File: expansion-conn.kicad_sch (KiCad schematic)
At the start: 6 parts, among them J1 J_ERM8-040-XX.X-X-DV-XX_SAMTEC

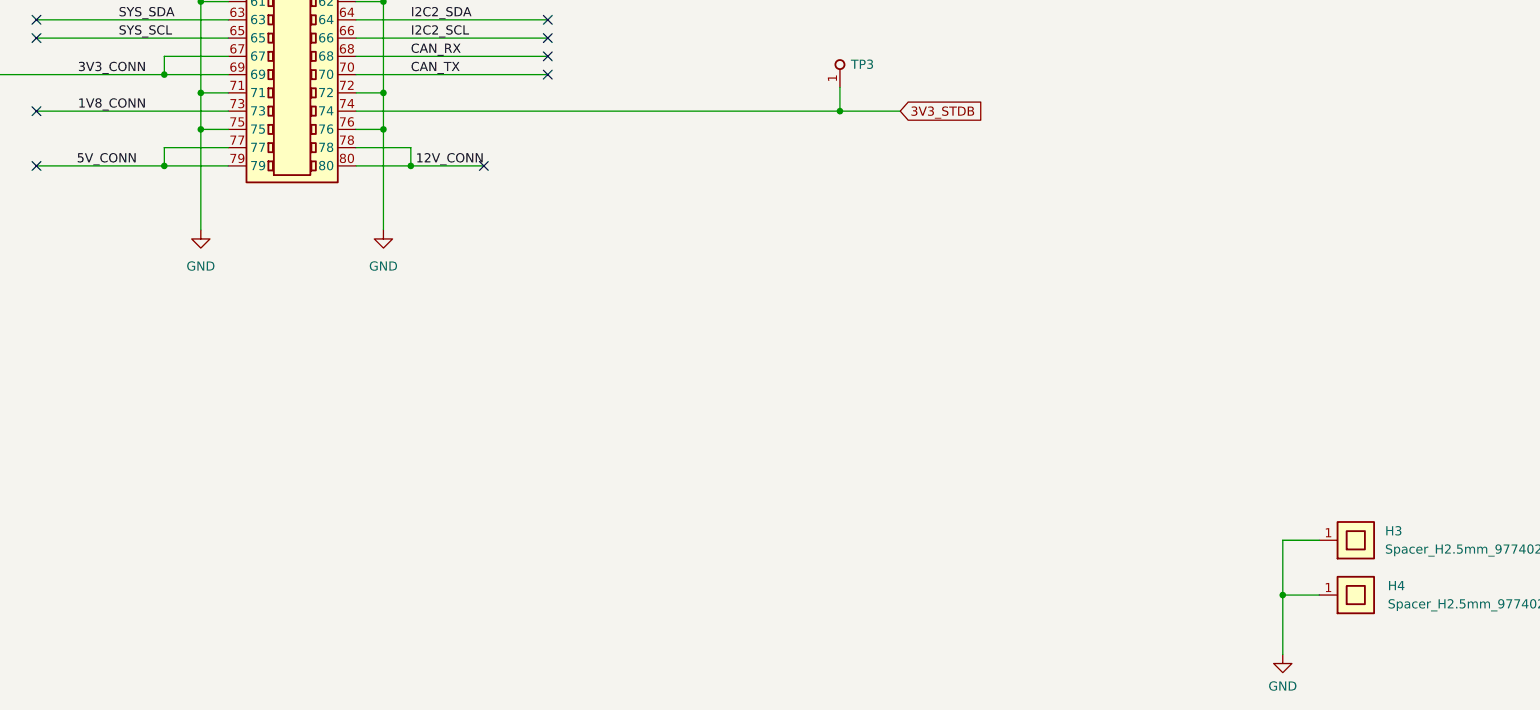
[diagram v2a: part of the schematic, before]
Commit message: [#45990] Fix silk screen drcs
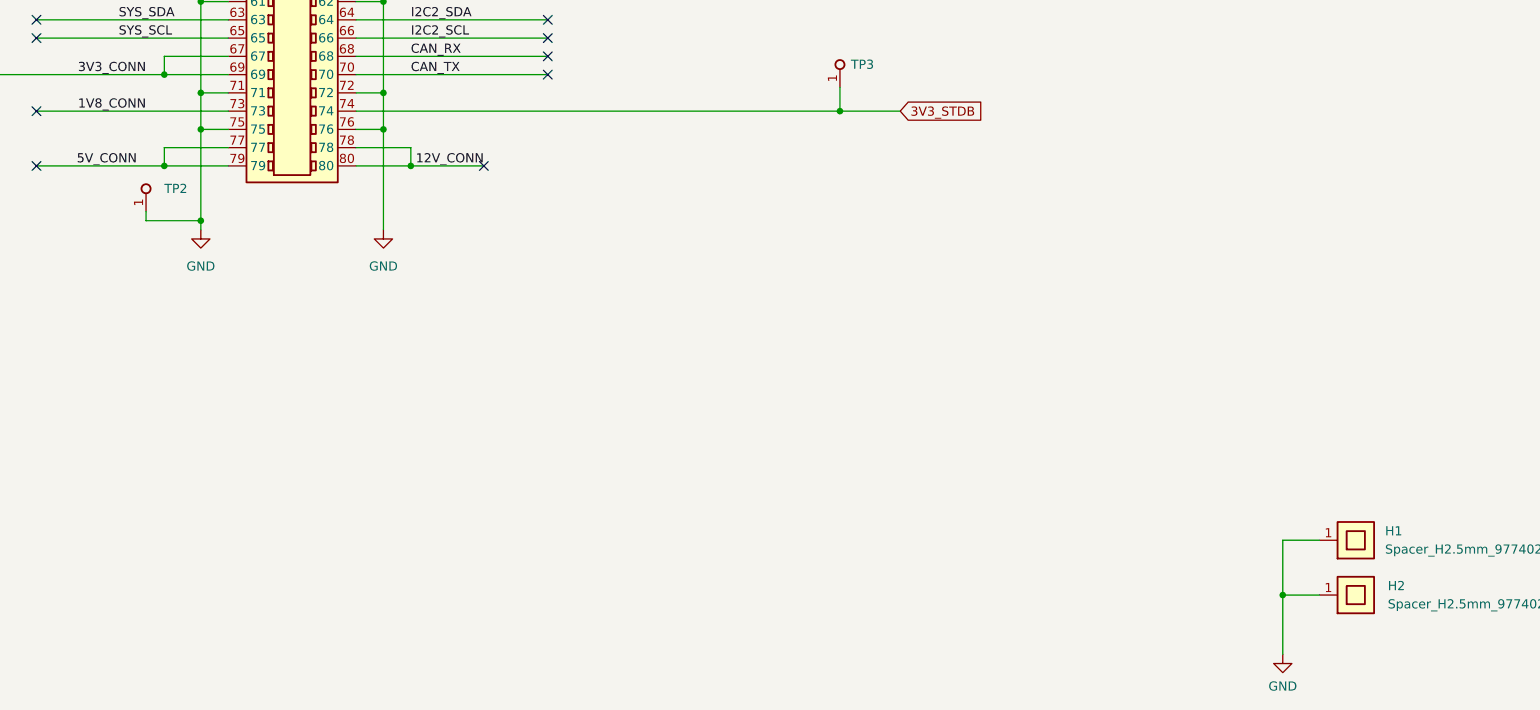
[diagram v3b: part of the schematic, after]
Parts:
- added TP2: TP_0.75mm_SMD, antmicro-footprints:TP_SMD_0.75mm, symbol antmicroTestPoints:TP_0.75mm_SMD
- renumbered H3 to H1, H4 to H2
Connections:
- net GND: now also TP2.1
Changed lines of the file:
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@@
   (junction (at 222.25 100.33) (diameter 0) (color 0 0 0 0)
   )
+  (junction (at 196.85 181.61) (diameter 0) (color 0 0 0 0)
+  )
   (junction (at 196.85 163.83) (diameter 0) (color 0 0 0 0)
   )
@@
     (stroke (width 0) (type default) (color 0 0 0 0))
   )
+  (wire (pts (xy 189.23 180.34) (xy 189.23 181.61))
+    (stroke (width 0) (type default) (color 0 0 0 0))
+  )
   (wire (pts (xy 173.99 148.59) (xy 200.66 148.59))
     (stroke (width 0) (type default) (color 0 0 0 0))
@@
     (stroke (width 0) (type default) (color 0 0 0 0))
   )
+  (wire (pts (xy 189.23 181.61) (xy 196.85 181.61))
+    (stroke (width 0) (type default) (color 0 0 0 0))
+  )
   (wire (pts (xy 173.99 133.35) (xy 200.66 133.35))
     (stroke (width 0) (type default) (color 0 0 0 0))
@@
     (stroke (width 0) (type default) (color 0 0 0 0))
   )
+  (wire (pts (xy 196.85 181.61) (xy 196.85 182.88))
+    (stroke (width 0) (type default) (color 0 0 0 0))
+  )
   (wire (pts (xy 173.99 118.11) (xy 200.66 118.11))
     (stroke (width 0) (type default) (color 0 0 0 0))
@@
     (stroke (width 0) (type default) (color 0 0 0 0))
   )
-  (wire (pts (xy 196.85 168.91) (xy 196.85 182.88))
+  (wire (pts (xy 196.85 168.91) (xy 196.85 181.61))
     (stroke (width 0) (type default) (color 0 0 0 0))
   )
@@
   (symbol (lib_id "antmicropower:GND") (at 347.345 241.935 0) (unit 1)
     (in_bom yes) (on_board yes) (fields_autoplaced)
-    (property "Reference" "#PWR0118" (id 0) (at 347.345 248.285 0)
+    (property "Reference" "#PWR05" (id 0) (at 347.345 248.285 0)
       (effects (font (size 1.27 1.27)) hide)
     )
@@
   (symbol (lib_id "antmicroMechanicalParts:Spacer_H2.5mm_9774025151") (at 352.425 233.68 0) (unit 1)
     (in_bom yes) (on_board yes) (fields_autoplaced)
-    (property "Reference" "H4" (id 0) (at 361.95 232.4099 0)
+    (property "Reference" "H2" (id 0) (at 361.95 232.4099 0)
       (effects (font (size 1.27 1.27) (thickness 0.15)) (justify left))
     )
@@
   (symbol (lib_id "antmicropower:GND") (at 222.25 182.88 0) (unit 1)
     (in_bom yes) (on_board yes) (fields_autoplaced)
-    (property "Reference" "#PWR06" (id 0) (at 222.25 189.23 0)
+    (property "Reference" "#PWR04" (id 0) (at 222.25 189.23 0)
       (effects (font (size 1.27 1.27)) hide)
     )
@@
     (pin "80")
   )
+  (symbol (lib_id "antmicroTestPoints:TP_0.75mm_SMD") (at 189.23 180.34 270) (mirror x) (unit 1)
+    (in_bom yes) (on_board yes) (fields_autoplaced)
+    (property "Reference" "TP2" (id 0) (at 191.77 177.1649 90)
+      (effects (font (size 1.27 1.27) (thickness 0.15)) (justify left))
+    )
+    (property "Value" "TP_0.75mm_SMD" (id 1) (at 181.61 165.1 0)
+      (effects (font (size 1.27 1.27) (thickness 0.15)) (justify left bottom) hide)
+    )
+    (property "Footprint" "antmicro-footprints:TP_SMD_0.75mm" (id 2) (at 179.07 165.1 0)
+      (effects (font (size 1.27 1.27) (thickness 0.15)) (justify left bottom) hide)
+    )
+    (property "Datasheet" "" (id 3) (at 176.53 165.1 0)
+      (effects (font (size 1.27 1.27) (thickness 0.15)) (justify left bottom) hide)
+    )
+    (property "MPN" "" (id 4) (at 189.23 180.34 0)
+      (effects (font (size 1.27 1.27)) hide)
+    )
+    (property "Manufacturer" "" (id 5) (at 189.23 180.34 0)
+      (effects (font (size 1.27 1.27)) hide)
+    )
+    (property "Author" "Antmicro" (id 6) (at 173.99 165.1 0)
+      (effects (font (size 1.27 1.27) (thickness 0.15)) (justify left bottom) hide)
+    )
+    (property "License" "Apache-2.0" (id 7) (at 171.45 165.1 0)
+      (effects (font (size 1.27 1.27) (thickness 0.15)) (justify left bottom) hide)
+    )
+    (pin "1")
+  )
   (symbol (lib_id "antmicroTestPoints:TP_0.75mm_SMD") (at 132.715 158.75 90) (unit 1)
     (in_bom yes) (on_board yes) (fields_autoplaced)
@@
   (symbol (lib_id "antmicropower:GND") (at 196.85 182.88 0) (unit 1)
     (in_bom yes) (on_board yes) (fields_autoplaced)
-    (property "Reference" "#PWR05" (id 0) (at 196.85 189.23 0)
+    (property "Reference" "#PWR03" (id 0) (at 196.85 189.23 0)
       (effects (font (size 1.27 1.27)) hide)
     )
@@
   (symbol (lib_id "antmicroMechanicalParts:Spacer_H2.5mm_9774025151") (at 352.425 226.06 0) (unit 1)
     (in_bom yes) (on_board yes) (fields_autoplaced)
-    (property "Reference" "H3" (id 0) (at 361.569 224.7899 0)
+    (property "Reference" "H1" (id 0) (at 361.569 224.7899 0)
       (effects (font (size 1.27 1.27) (thickness 0.15)) (justify left))
     )

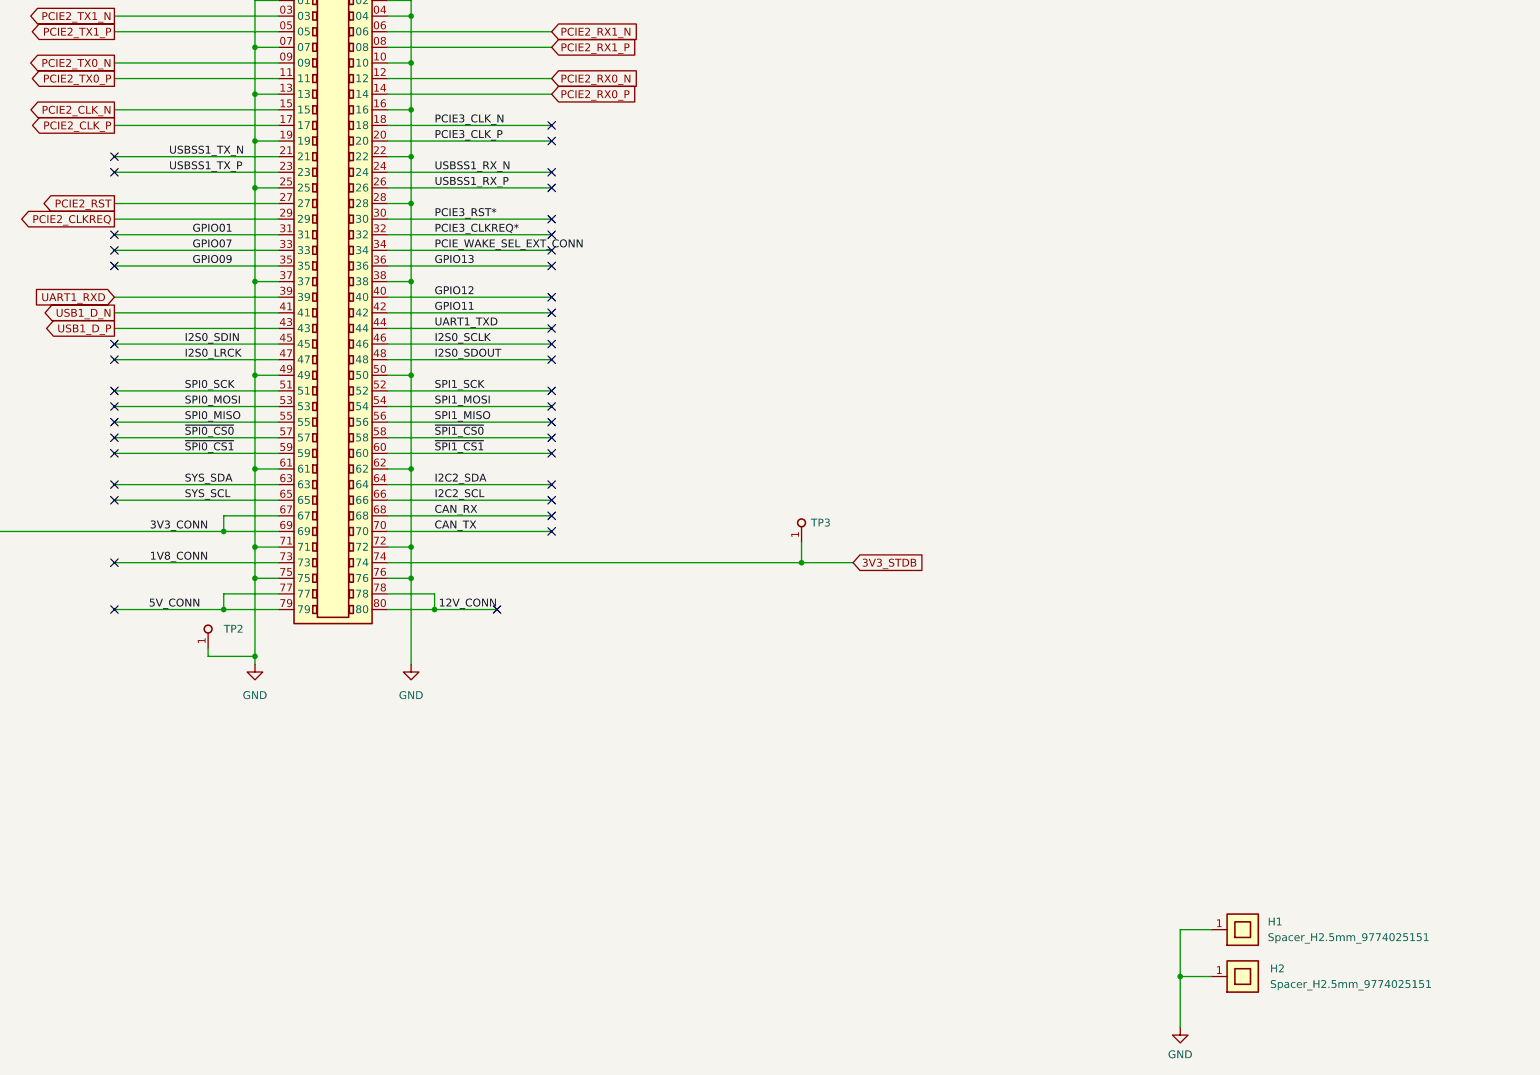
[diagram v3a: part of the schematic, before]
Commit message: [#45990] Cosmetic changes for schematic, expand README
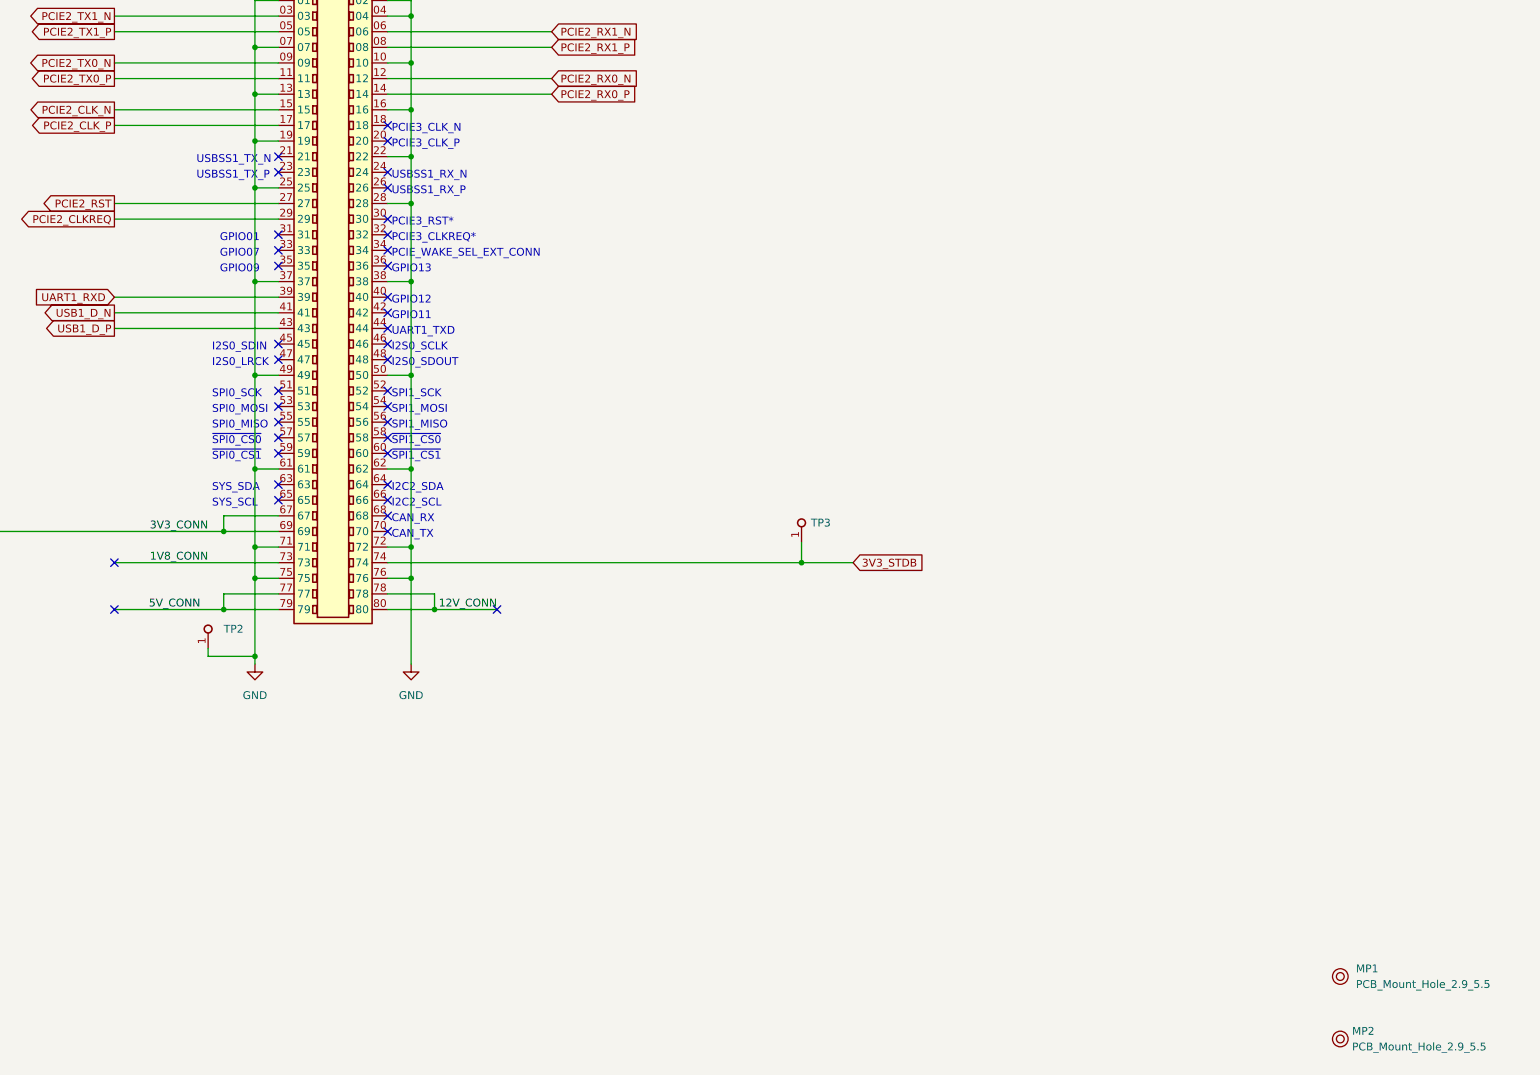
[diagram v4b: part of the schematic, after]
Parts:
- removed H1, H2: Spacer_H2.5mm_9774025151, antmicro-footprints:Spacer_SMD_M2.5_H2.5mm_Wurth_9774025151, symbol antmicroMechanicalParts:Spacer_H2.5mm_9774025151
- added MP1, MP2: PCB_Mount_Hole_2.9_5.5, antmicro-footprints:mounting-hole-2.9mm-5.5mm, symbol antmicroMechanicalParts:PCB_Mount_Hole_2.9_5.5
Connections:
- net CAN_RX: no longer names the net of J1.68
- net CAN_TX: no longer names the net of J1.70
- net GPIO01: no longer names the net of J1.31
- net GPIO07: no longer names the net of J1.33
- net GPIO09: no longer names the net of J1.35
- net GPIO11: no longer names the net of J1.42
- net GPIO12: no longer names the net of J1.40
- net GPIO13: no longer names the net of J1.36
- net I2C2_SCL: no longer names the net of J1.66
- net I2C2_SDA: no longer names the net of J1.64
- net I2S0_LRCK: no longer names the net of J1.47
- net I2S0_SCLK: no longer names the net of J1.46
- net I2S0_SDIN: no longer names the net of J1.45
- net I2S0_SDOUT: no longer names the net of J1.48
- net PCIE3_CLKREQ*: no longer names the net of J1.32
- net PCIE3_CLK_N: no longer names the net of J1.18
- net PCIE3_CLK_P: no longer names the net of J1.20
- net PCIE3_RST*: no longer names the net of J1.30
- net PCIE_WAKE_SEL_EXT_CONN: no longer names the net of J1.34
- net SPI0_MISO: no longer names the net of J1.55
- net SPI0_MOSI: no longer names the net of J1.53
- net SPI0_SCK: no longer names the net of J1.51
- net SPI1_MISO: no longer names the net of J1.56
- net SPI1_MOSI: no longer names the net of J1.54
- net SPI1_SCK: no longer names the net of J1.52
- net SYS_SCL: no longer names the net of J1.65
- net SYS_SDA: no longer names the net of J1.63
- net UART1_TXD: no longer names the net of J1.44
- net USBSS1_RX_N: no longer names the net of J1.24
- net USBSS1_RX_P: no longer names the net of J1.26
- net USBSS1_TX_N: no longer names the net of J1.21
- net USBSS1_TX_P: no longer names the net of J1.23
- net ~{SPI0_CS0}: no longer names the net of J1.57
- net ~{SPI0_CS1}: no longer names the net of J1.59
- net ~{SPI1_CS0}: no longer names the net of J1.58
- net ~{SPI1_CS1}: no longer names the net of J1.60
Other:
- note added: "CAN_RX"
- note added: "CAN_TX"
- note added: "GPIO01"
- note added: "GPIO07"
- note added: "GPIO09"
- note added: "GPIO11"
- note added: "GPIO12"
- note added: "GPIO13"
- note added: "I2C2_SCL"
- note added: "I2C2_SDA"
- note added: "I2S0_LRCK"
- note added: "I2S0_SCLK"
- note added: "I2S0_SDIN"
- note added: "I2S0_SDOUT"
- note added: "PCIE3_CLKREQ*"
- note added: "PCIE3_CLK_N"
- note added: "PCIE3_CLK_P"
- note added: "PCIE3_RST*"
- note added: "PCIE_WAKE_SEL_EXT_CONN"
- note added: "SPI0_MISO"
- note added: "SPI0_MOSI"
- note added: "SPI0_SCK"
- note added: "SPI1_MISO"
- note added: "SPI1_MOSI"
- note added: "SPI1_SCK"
- note added: "SYS_SCL"
- note added: "SYS_SDA"
- note added: "UART1_TXD"
- note added: "USBSS1_RX_N"
- note added: "USBSS1_RX_P"
- note added: "USBSS1_TX_N"
- note added: "USBSS1_TX_P"
- note added: "~{SPI0_CS0}"
- note added: "~{SPI0_CS1}"
- note added: "~{SPI1_CS0}"
- note added: "~{SPI1_CS1}"
